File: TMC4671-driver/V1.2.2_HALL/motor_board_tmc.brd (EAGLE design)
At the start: 60 x 110 mm, 164 parts, among them U1 TMC4671, U10 BSC030N08NS5ATMA1, U11 BSC030N08NS5ATMA1, U12 BSC030N08NS5ATMA1, U13 BSC030N08NS5ATMA1, U14 MCP14XX, U15 BSC030N08NS5ATMA1, U16 BSC030N08NS5ATMA1, U17 BSC030N08NS5ATMA1, U18 NC7NZ17K8X-3-BUFFER, U19 NC7NZ17K8X-3-BUFFER, U2 LM5109BSD, U20 LM74700-Q1, U22 BSC030N08NS5ATMA1, U23 MAX5033BASA+T, U24 AP3012KTR-G1, U3 LM5109BSD, U4 LM5109BSD, U5 LM5109BSD, U6 BSC030N08NS5ATMA1, U7 BSC030N08NS5ATMA1, U8 AD841X, U9 AD841X, X1 2516-, X2 GMSTBA4, X3 GMSTBA4, Y1 25MHz

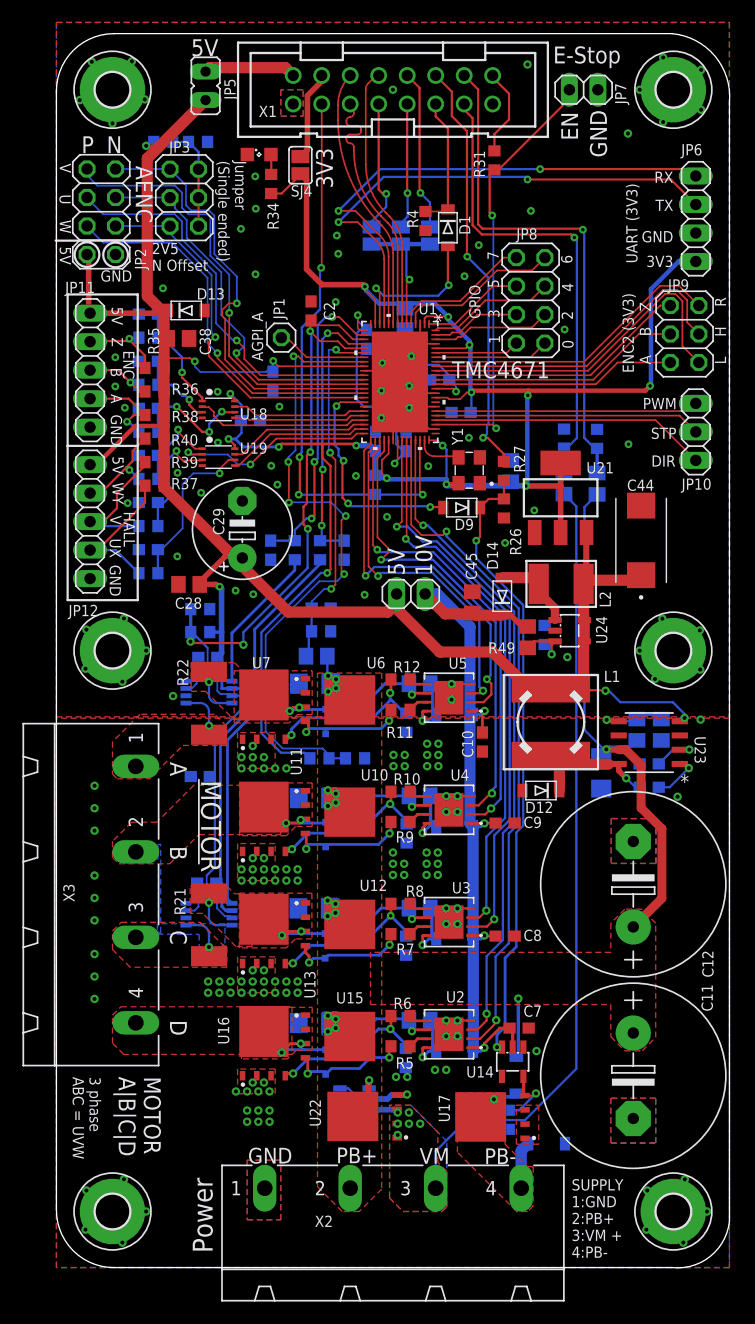
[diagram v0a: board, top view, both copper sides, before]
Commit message: Added files for Hall sensor TMC
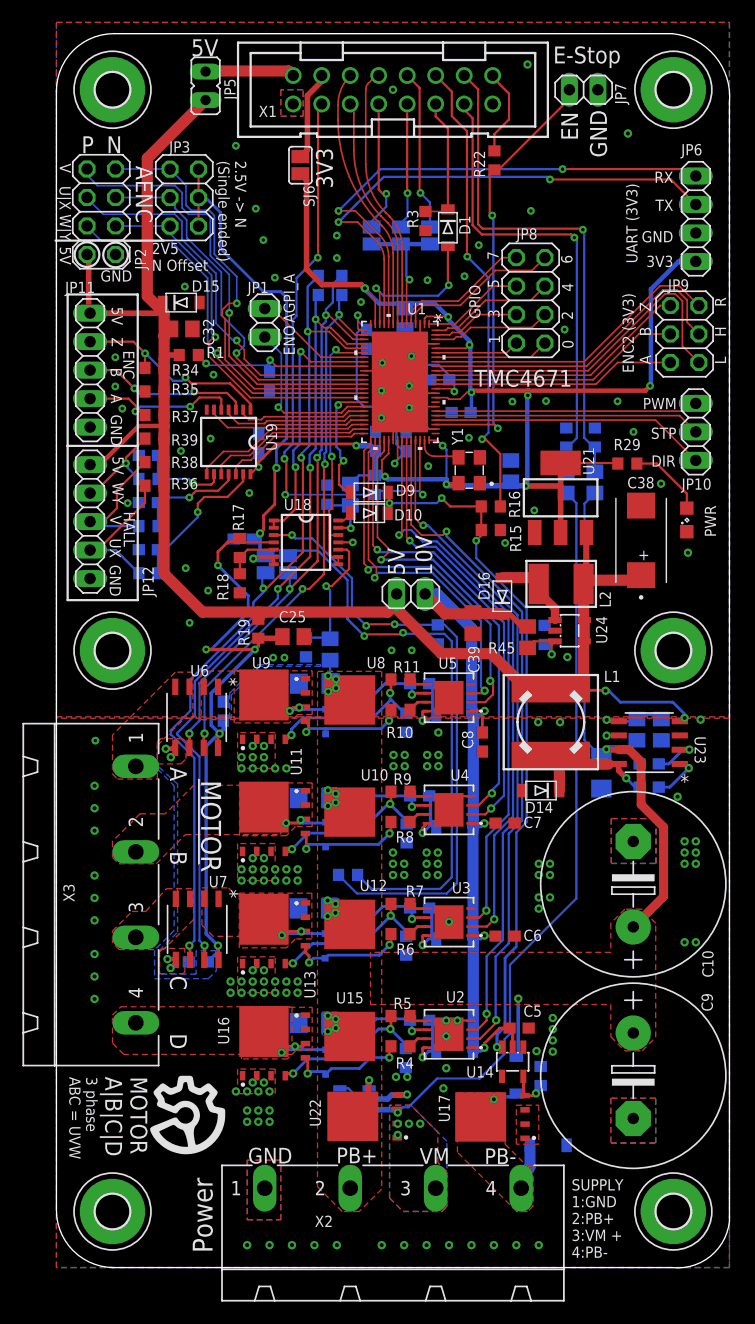
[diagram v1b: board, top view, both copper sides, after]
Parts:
- removed C40: 4.7µF, resistor:C0805
- removed C41, C42: 100nF, resistor:C0603
- removed C43: 1µF, resistor:C1206
- removed C44: 593D476X0016D2TE3, Powermisc:CAPPM7343X310N
- removed C45: 4.7µF <REMOVE>, resistor:C0805
- removed R47: 294k, resistor:R0805
- removed R48, R49: 71.5k, resistor:R0805
- removed R50: 10k, resistor:R0603
- removed R51: 33k, resistor:R0603
- added D16: LV low drop, adafruit:SOD-123FL
- added SJ5: (no value), jumper:SJ
- added SJ6: 3.3V, jumper:SJ
- C10, C9: value 100nF -> 680µF; device resistor:C0603 -> resistor:E7,5-16
- C11, C12: value 680µF -> 1µF; device resistor:E7,5-16 -> resistor:C1206
- C15, C16: value 1µF -> 100nF; device resistor:C1206 -> resistor:C0603
- C18: value 100nF -> 4.7µF; device resistor:C0603 -> resistor:C0805
- C20: value 4.7µF -> 100nF; device resistor:C0805 -> resistor:C0603
- C21, C22, C23, C24: device resistor:C0805 -> resistor:C0603
- C25: value 1n -> 4.7µF; device resistor:C0603 -> resistor:C0805
- C26: value 100nF -> 100n
- C27: value 100nF -> 1n
- C28: value 4.7µF -> 1n; device resistor:C0805 -> resistor:C0603
- C29: value (none) -> 1n; device resistor:E5-8,5 -> resistor:C0603
- C32, C34: value 100p -> 4.7µF; device resistor:C0603 -> resistor:C0805
- C33, C35: value 1n -> 100nF
- C36: value 100p -> 100nF
- C37: value 1n -> 1µF; device resistor:C0603 -> resistor:C1206
- C38: value 4.7µF -> 593D476X0016D2TE3; device resistor:C0805 -> Powermisc:CAPPM7343X310N
- C39: value 100nF -> 4.7µF
- D10: value BZX384-XXX -> LV low drop; device Powermisc:SOD323-R -> adafruit:SOD-123FL
- D11: value HV >100V -> BZX384-XXX; device adafruit:SOD-123FL -> Powermisc:SOD323-R
- D13: value 5.6V zener -> Zener 65V (MMSZ5265BT1G)
- D14: value LV low drop -> HV >100V
- D15: value Zener 65V (MMSZ5265BT1G) -> 5.6V zener
- JP1: device pinhead:1X01 -> pinhead:1X02
- R1, R19, R4: value 10k -> 2.2
- R12: value 2.2 -> 33k
- R13: value 71.5k -> 33k; device resistor:R0805 -> resistor:R0603
- R14: value 1.5k -> 33k
- R15, R18: value 294k -> 10k; device resistor:R0805 -> resistor:R0603
- R16: value 10k -> 1.5k
- R17, R28: value 33k -> 10k
- R21: value 1.5m -> 33k; device resistor:R2512 -> resistor:R0603
- R22: value 1.5m -> 1.5k; device resistor:R2512 -> resistor:R0603
- R23, R44, R45: value 1.5k -> 71.5k; device resistor:R0603 -> resistor:R0805
- R25: value 33k -> 294k; device resistor:R0603 -> resistor:R0805
- R27, R43: value 1.5k -> 294k; device resistor:R0603 -> resistor:R0805
- R29: value 22k thermistor -> 1.5k
- R30: value 1.5k -> 10k thermistor
- R32: value 10k -> 71.5k; device resistor:R0603 -> resistor:R0805
- R33: value 10k -> 47k
- R34: value 330 -> 4.7k
- R40: value 4.7k -> 1.5k
- R46: value 1.5k -> 10k
- SJ4: value 3.3V -> (none)
- U18: value NC7NZ17K8X-3-BUFFER -> MCP6004; device Powermisc:VFSOP-8 -> Powermisc:TSSOP14
- U19: value NC7NZ17K8X-3-BUFFER -> 74LV17APWJ; device Powermisc:VFSOP-8 -> Powermisc:TSSOP14
- U6, U7: value BSC030N08NS5ATMA1 -> TMCS1100; device OHSC_Power:MOSFET_BSC093N04LSGATMA1 -> Powermisc:SOIC8_D_TEX
- U8, U9: value AD841X -> BSC030N08NS5ATMA1; device Powermisc:MSOP8 -> OHSC_Power:MOSFET_BSC093N04LSGATMA1
- moved D15 81.7 mm to (11.1, -24.0), flipped to the top, turned to 0 degrees
- moved D13 81.1 mm to (43.9, -99.1), flipped to the bottom, turned to 180 degrees
- moved R4 73.6 mm to (30.7, -90.3), turned to 0 degrees
- moved C5 62.9 mm to (41.2, -88.7), flipped to the top, turned to 180 degrees
- moved R44 57.6 mm to (53.9, -62.0), turned to 270 degrees
- moved R28 57.1 mm to (45.5, -36.0), turned to 270 degrees
- moved C36 56.0 mm to (52.9, -67.2), turned to 0 degrees
- moved C33 55.0 mm to (26.2, -98.0)
- moved R22 54.7 mm to (39.0, -11.3)
- moved C27 54.6 mm to (25.4, -22.4), turned to 270 degrees
- moved C20 52.5 mm to (32.4, -78.0), turned to 0 degrees
- moved C16 51.9 mm to (18.1, -36.5), turned to 90 degrees
- moved C19 51.7 mm to (32.4, -88.0), turned to 0 degrees
- moved C35 50.4 mm to (52.9, -65.1)
- moved LED1 50.1 mm to (56.2, -43.4), turned to 90 degrees
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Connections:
- removed net N$10: R24.2, U9.5
- removed net N$11: JP11.2, R35.1, R44.2
- removed net N$22: JP3.2, JP3.4, JP3.6, R32.1, R33.2
- removed net N$6: R23.2, U8.5
- removed net N$7: JP11.4, R38.1, R46.2
- removed net N$9: JP11.3, R36.1, R45.2
- removed net V_SENSE/2: C1.2, C2.2, R1.1, R2.2, U1.17, U1.19, U8.3, U8.7, U9.3, U9.7
- new net 2.5V_REF: C26.1, JP3.2, JP3.4, JP3.6, R30.2, SJ1.1, SJ2.1, U18.6, U18.7
- new net 2.5V_REF_A: C27.1, SJ1.2, U1.17, U6.6
- new net 2.5V_REF_C: C28.1, SJ2.2, U1.19, U7.6
- new net 2.5V_REF_RAW: R17.1, R18.2, U18.5
- new net 5V_ADC: C2.2, R1.1, U1.23
- new net 5V_SENSE: C23.2, C24.1, C25.1, R17.2, R19.1, U18.4, U6.8, U7.8
- new net BRAKE_RES_COMP: D10.A, U18.14
- new net BRAKE_RES_TH: R32.1, R33.2, U18.13
- new net TH_FET: R30.1, R31.2, U18.3
- new net V_INT_TMC_RAW: R23.1, R24.2, U18.10
- net +3V3: now also C15.1, C16.1, C34.1, R2.2, R32.2, SJ6.2, U19.14; no longer C19.1, C20.1, C40.1, R3.2, R34.2, SJ4.2, U18.P$8, U19.P$8
- net +5V: now also C32.1, D15.C, R19.2, R34.2; no longer C26.1, C27.1, C28.1, C29.+, C4.2, C44.1, D13.C, R32.2, R40.2, U1.23, U8.6, U9.6
- net AGPI_A: now also JP1.2; no longer JP1.1
- net AGPI_B: now also U18.1, U18.2; no longer R29.1, R30.2
- net BRAKE_CTRL: now also D10.C, R15.2, R16.2; no longer R26.2, R27.2
- net BRAKE_CTRL_EXT: now also R16.1; no longer R27.1
- net BRAKE_GATE: now also R21.2; no longer R51.2
- net CS1: now also SJ3.1; no longer SJ1.1
- net CS2: now also SJ4.1; no longer SJ2.1
- net CS3: now also SJ5.1; no longer SJ3.1
- net CS_TMC: now also SJ4.2, SJ5.2; no longer SJ1.2, SJ2.2
- net ENABLE: now also R22.1; no longer R31.1
- net ENC_A: now also U19.6; no longer U18.P$2
- net ENC_A_5V: now also JP11.4, R37.1, U19.5; no longer C36.2, R46.1, U18.P$6
- net ENC_B: now also U19.4; no longer U18.P$5
- net ENC_B_5V: now also JP11.3, R35.1, U19.3; no longer C34.2, R45.1, U18.P$3
- net ENC_Z: now also U19.2; no longer U18.P$7
- net ENC_Z_5V: now also JP11.2, R34.1, U19.1; no longer C32.2, R44.1, U18.P$1
- net ENO: now also JP1.1
- net FLAG: now also R3.2; no longer R4.2
- net GND: now also C10.-, C11.2, C12.2, C23.1, C24.2, C29.1, C32.2, C34.2, C39.2, C9.-, D14.A, R12.1, R13.1, R15.1, R18.1, R21.1, R24.1, R3.1, R31.1, R44.2, R46.1, U18.11, U19.7, U6.5, U7.5, U9.1, U9.3; no longer C10.1, C11.-, C12.-, C19.2, C20.2, C27.2, C28.2, C29.-, C32.1, C33.1, C34.1, C36.1, C40.2, C41.1, C43.1, C44.2, C45.2, C9.1, D12.A, R16.1, R17.1, R19.1, R2.1, R25.1, R30.1, R4.1, R48.2, R50.1, R51.1, U18.P$4, U19.P$4, U7.1, U7.2, U7.3, U8.2
- net G_HS_A: now also R10.1, U8.4; no longer R11.1, U6.4
- net G_HS_B: now also R8.1; no longer R9.1
- net G_HS_C: now also R6.1; no longer R7.1
- net G_HS_D: now also D11.C, R4.1; no longer D10.C, R5.1
- net G_LS_A: now also R11.1, R12.2, U9.4; no longer R12.1, R17.2, U7.4
- net G_LS_B: now also R13.2, R9.1; no longer R10.1, R20.2
- net G_LS_C: now also R14.2, R7.1; no longer R25.2, R8.1
- net G_LS_D: now also R20.2, R5.1; no longer R28.2, R6.1
- net HALL_UX: now also U19.12; no longer U19.P$2
- net HALL_UX_5V: now also C29.2, R40.1, U19.13; no longer C33.2, R41.1, U19.P$6
- net HALL_V: now also U19.10; no longer U19.P$5
- net HALL_V_5V: now also C30.2, R41.1, U19.11; no longer C35.2, R42.1, U19.P$3
- net HALL_WY: now also U19.8; no longer U19.P$7
- net HALL_WY_5V: now also C31.2, R42.1, U19.9; no longer C37.2, R43.1, U19.P$1
- net MOT_A: now also C22.2, U8.1, U8.2, U8.3, U9.5; no longer C24.2, R22.2, U6.3, U7.5, U8.8
- net MOT_A_OUT: now also U6.3, U6.4; no longer R22.1, U8.1
- net MOT_B: now also C21.2; no longer C23.2
- net MOT_C: now also C20.2, U7.1, U7.2; no longer C22.2, R21.2, U9.8
- net MOT_C_OUT: now also U7.3, U7.4; no longer R21.1, U9.1
- net MOT_D: now also C19.2, D11.A; no longer C21.2, D10.A
- net N$1: now also R36.1, R40.2; no longer R37.1, R41.2
- net N$12: now also D16.A; no longer D14.A
- net N$13: now also R11.2; no longer R12.2
- net N$15: now also R39.1, R42.2; no longer R40.1, R43.2
- net N$16: now also C36.2, D14.C; no longer C42.2, D12.C
- net N$17: now also R22.2; no longer R31.2
- net N$18: now also C22.1; no longer C24.1
- net N$19: now also C36.1; no longer C42.1
- net N$20: now also SJ6.1; no longer SJ4.1
- net N$21: now also R43.1, R44.1; no longer R47.1, R48.1
- net N$24: now also C33.1; no longer C39.1
- net N$25: now also C35.2; no longer C41.2
- net N$27: now also R10.2; no longer R11.2
- net N$28: now also C21.1; no longer C23.1
- net N$29: now also R9.2; no longer R10.2
- net N$3: now also R38.1, R41.2; no longer R39.1, R42.2
- net N$30: now also R8.2; no longer R9.2
- net N$31: now also C19.1; no longer C21.1
- net N$32: now also R5.2; no longer R6.2
- net N$33: now also R4.2; no longer R5.2
- net N$34: now also C20.1; no longer C22.1
- net N$35: now also R7.2; no longer R8.2
- net N$36: now also R6.2; no longer R7.2
- net N$5: now also R45.1, R46.2; no longer R49.1, R50.2
- net N$8: now also R29.1; no longer R34.1
- net RESET: now also R2.1; no longer R3.1
- net RES_FET: now also D12.A, D13.C; no longer D11.A, D15.C
- net SENSE_A: now also C27.2, U6.7; no longer C30.2, R23.1
- net SENSE_C: now also C28.2, U7.7; no longer C31.2, R24.1
- net V+: now also C10.+, C11.1, C12.1, C37.2, C9.+, D12.C, R23.2, R25.2, R43.2, U8.5; no longer C11.+, C12.+, C15.1, C16.1, C43.2, D11.C, R13.2, R15.2, R47.2, U6.5
- net VCORE: now also C1.2, C4.2; no longer C5.2, C6.2
- net V_EXT: now also R27.1, R28.2; no longer R18.1, R19.2
- net V_GD: now also C39.1, C5.2, C6.2, D16.C, R45.2; no longer C10.2, C45.1, C9.2, D14.C, R49.2
- net V_INT: now also R25.1, R26.2; no longer R15.1, R16.2
- net V_INT_TMC: now also U18.12, U18.8, U18.9; no longer C25.1, R13.1, R14.2
- net V_MOT_IN: now also C33.2, R27.2; no longer C39.2, R18.2
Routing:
- net 2.5V_REF: track 0.00 -> 100.2 mm, vias 0 -> 5
- net V_SENSE/2: track 87.8 -> 0.00 mm, vias 5 -> 0
- net 2.5V_REF_C: track 0.00 -> 75.1 mm, vias 0 -> 4
- net 5V_SENSE: track 0.00 -> 60.2 mm, vias 0 -> 5
- net +5V: track 205.0 -> 146.8 mm, vias 6 -> 2
- net TH_FET: track 0.00 -> 55.5 mm, vias 0 -> 3
- net 2.5V_REF_A: track 0.00 -> 53.6 mm, vias 0 -> 4
- net SENSE_C: track 24.6 -> 70.8 mm, vias 3 -> 4
- net +3V3: track 181.4 -> 143.7 mm, vias 15 -> 12
- net N$10: track 34.2 -> 0.00 mm
- net AGPI_B: track 57.1 -> 23.4 mm, vias 5 -> 2
- net SENSE_A: track 27.6 -> 49.1 mm, vias 3 -> 4
- net 5V_ADC: track 0.00 -> 16.8 mm, vias 0 -> 2
- net ENO: track 0.00 -> 15.1 mm, vias 0 -> 1
- net N$6: track 13.1 -> 0.00 mm
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- added copper zone on layer 1, net GND1
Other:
- board text added: "2.5V -> N (Single ended)"
- board text added: "2V5-REF Sense"
- board text added: "BR_TH"
- board text added: "ENCODER"
- board text added: "ENO"
- board text added: "PWR"
- board text added: "Supply: PSU (protected): VM (+) and GND (-) ALWAYS connect braking resistor between PB+ (Internal motor supply) and PB-"
- board text added: "U|X"
- board text added: "V1.3 - YR 2021"
- board text added: "VEXT"
- board text added: "VINT"
- board text added: "W|Y"
- board text removed: "Jumper (Single ended)"
- board text removed: "Supply: PSU (protected): VM (+) and GND (-) ALWAYS use braking resistor between PB+ and PB Battery: PB+ (+) and GND (-) No resistor"
- board text removed: "V1.2.1 - YR 2021"
